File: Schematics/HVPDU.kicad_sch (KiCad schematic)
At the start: 11 parts, among them J35 BAMOCAR, J36 MCU CAN, J37 MCU COM, J38 3-2325013-1, J39 Energy Meter Current, J40 PL00X-301-10M8, J41 PL00Y-301-10M8, J42 HVD, J43 MCU Resolver, J44 Energy Meter Voltage, J45 Energy meter COM port

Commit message: Revise charger and HVPDU schematics
Updates the KiCad projects for Charger and Schematics with substantial schematic rework: replaces the AVR ISP header with a dedicated AVR-ISP-6 symbol, adjusts wiring/net labels and power symbols, adds new indicator/connectivity elements, and repositions components in HV iso and connector sheets. The HVPDU sheet is expanded to A3 and reorganized with additional connector/library symbol definitions and updated interconnect mapping. This commit also includes newly generated schematic backups and an exported HVPDU PDF.
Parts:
- added J46: DCDC HV side, symbol Connector_Generic:Conn_01x02
- added J47: DCDC LV Side, symbol Connector_Generic:Conn_01x02
- added J48: CCCV IN, symbol Connector_Generic:Conn_01x02
- added J49: CCCV OUT, symbol Connector_Generic:Conn_01x02
- added J50: RT00122PNH03, symbol Connector_Generic:Conn_01x02
- added J51: TSAL_R, symbol Connector_Generic:Conn_01x02
- added J52: TSMP+, symbol Connector_Generic:Conn_01x01
- added J53: TSMP-, symbol Connector_Generic:Conn_01x01
- added J54: GLVMP, symbol Connector_Generic:Conn_01x01
- added J57: DHAB S/106, symbol Connector_Generic:Conn_01x04
- added J58: 12V power plug, symbol Connector_Generic:Conn_01x08
- added J59: GND PLUG, symbol Connector_Generic:Conn_01x08
- added K6: DISCHARGE RELAY GIGAVAC PNC113BDA, symbol Relay:Relay_SPST-NC
- added R6: 1k5, symbol Device:R
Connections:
- net +12V: now also J45.4 (Pin_4), J58.1 (Pin_1), J58.2 (Pin_2), J58.3 (Pin_3), J58.4 (Pin_4), J58.5 (Pin_5), J58.6 (Pin_6), J58.7 (Pin_7), J58.8 (Pin_8); no longer J45.1 (Pin_1)
- net GND: now also J45.1 (Pin_1), J57.3 (Pin_3), J59.1 (Pin_1), J59.2 (Pin_2), J59.3 (Pin_3), J59.4 (Pin_4), J59.5 (Pin_5), J59.6 (Pin_6), J59.7 (Pin_7), J59.8 (Pin_8), K6.A2
- net SDC_Relay: now also K6.A1
- net TS+: now reaches J35.1 (Pin_1), J40.1 (Pin_1), J44.1 (Pin_1)
- net TS+: now also J46.1 (Pin_1), J51.1 (Pin_1), J52.1 (Pin_1), K6.12
- net TS-: now reaches J35.5 (Pin_5), J39.1 (Pin_1)
- net TS-: now also J46.2 (Pin_2), J51.2 (Pin_2), J53.1 (Pin_1), R6.1
- net FS_CAN_L: now reaches J45.2 (Pin_2)
- net FS_CAN_H: now reaches J45.3 (Pin_3)
- new net: J49.1 (Pin_1), J50.1 (Pin_1)
- new net: J49.2 (Pin_2), J50.2 (Pin_2)
- new net: J47.1 (Pin_1), J48.1 (Pin_1)
- new net: J47.2 (Pin_2), J48.2 (Pin_2)
- new net: K6.11, R6.2
- new net +5V: J57.1 (Pin_1)
- new net Current High: J57.2 (Pin_2)
- new net Current Low: J57.4 (Pin_4)
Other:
- note added: "Accum"
- note added: "BSPD"
- note added: "FS DATALOGGER"
- note added: "LVB"
- note added: "MCU Energy Meter TSAL_R TSAL_G"
- note added: "MCU Energy Meter TSAL_R TSAL_G GLVMP-"
- note added: "Main Hoop"
- note added: "Motor shit"
- note added: "VCU"
- moved on the sheet: J36, J37, J38, J43, J44, J45

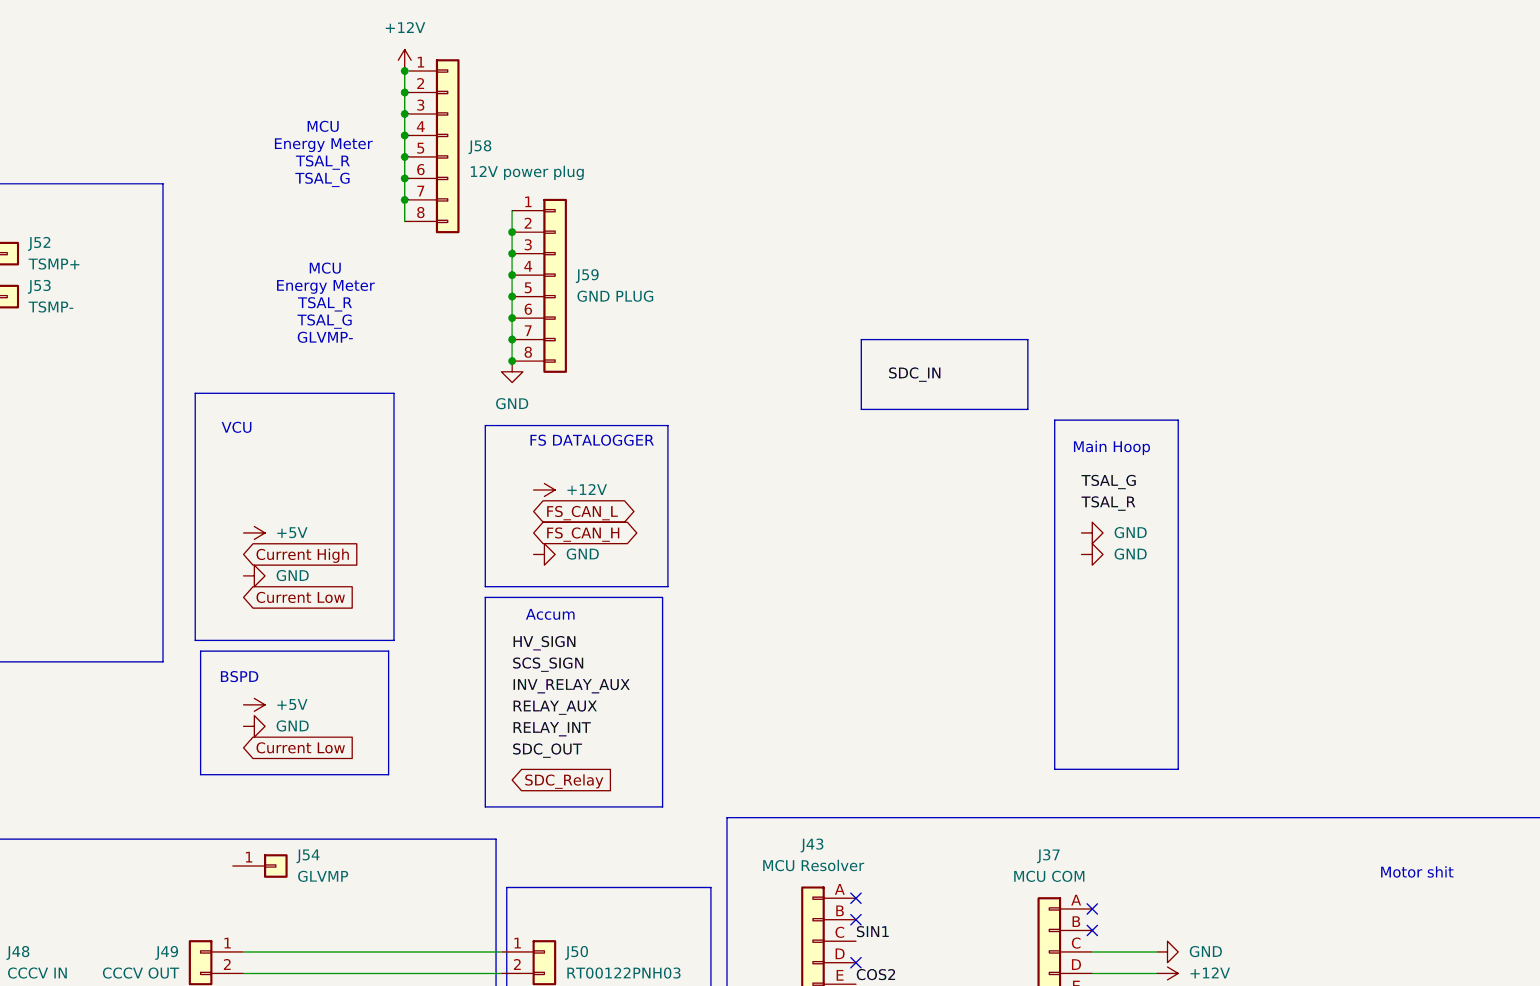
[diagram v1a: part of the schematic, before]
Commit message: Rework HVPDU and VCU connector wiring
Updates the HVPDU schematic with new connector symbols/instances (J55–J65), added MCU/FS CAN labels, and repositioned wiring blocks and labels. In VCU V3.3, the SRU/connector schematics and PCB were updated to reroute signals, rename the IGN_12V line to DIN_4, swap optocoupler value references to ELQ3H7, and realign many footprints/tracks; KiCad project metadata and 3D model references were also refreshed to KICAD10 paths. This change set also includes newly generated schematic backup ZIP archives.
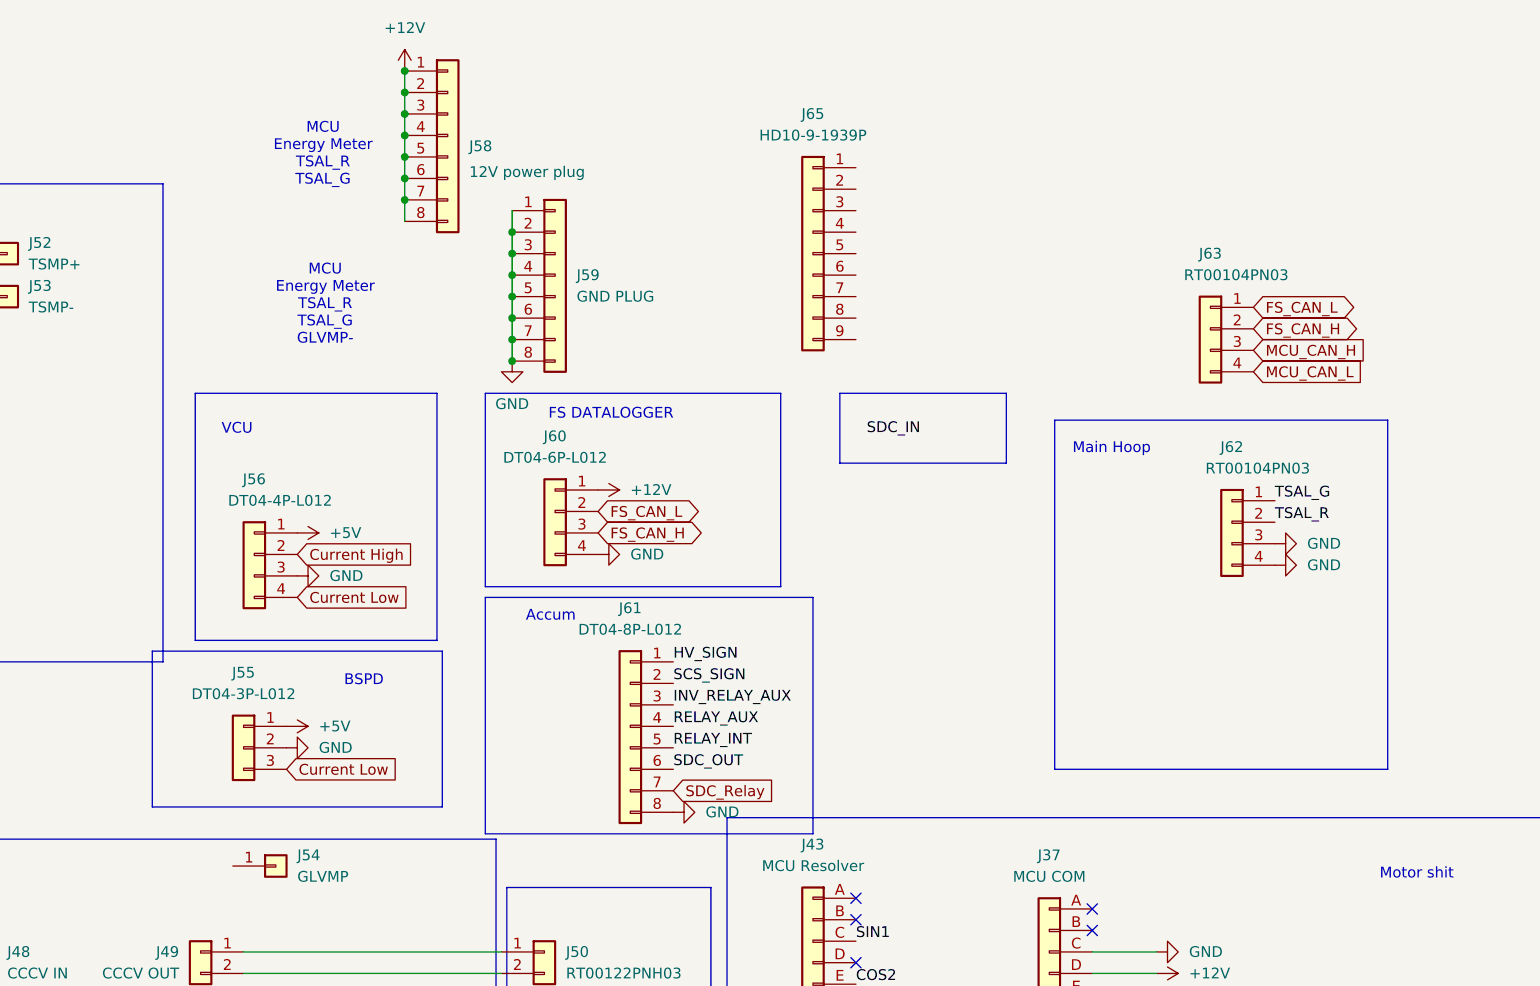
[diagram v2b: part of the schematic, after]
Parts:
- added J55: DT04-3P-L012, symbol Connector_Generic:Conn_01x03
- added J56: DT04-4P-L012, symbol Connector_Generic:Conn_01x04
- added J60: DT04-6P-L012, symbol Connector_Generic:Conn_01x04
- added J61: DT04-8P-L012, symbol Connector_Generic:Conn_01x08
- added J62, J63: RT00104PN03, symbol Connector_Generic:Conn_01x04
- added J65: HD10-9-1939P, symbol Connector_Generic:Conn_01x09
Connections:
- net +12V: now also J60.1 (Pin_1)
- net +5V: now also J55.1 (Pin_1), J56.1 (Pin_1)
- net Current High: now also J56.2 (Pin_2)
- net Current Low: now also J55.3 (Pin_3), J56.4 (Pin_4)
- net FS_CAN_H: now also J60.3 (Pin_3), J63.2 (Pin_2)
- net FS_CAN_L: now also J60.2 (Pin_2), J63.1 (Pin_1)
- net GND: now also J55.2 (Pin_2), J56.3 (Pin_3), J60.4 (Pin_4), J61.8 (Pin_8), J62.3 (Pin_3), J62.4 (Pin_4)
- net HV_SIGN: now also J61.1 (Pin_1)
- net INV_RELAY_AUX: now also J61.3 (Pin_3)
- net MCU_CAN_H: now also J63.3 (Pin_3)
- net MCU_CAN_L: now also J63.4 (Pin_4)
- net RELAY_AUX: now also J61.4 (Pin_4)
- net RELAY_INT: now also J61.5 (Pin_5)
- net SCS_SIGN: now also J61.2 (Pin_2)
- net SDC_OUT: now also J61.6 (Pin_6)
- net SDC_Relay: now also J61.7 (Pin_7)
- net TSAL_G: now also J62.1 (Pin_1)
- net TSAL_R: now also J62.2 (Pin_2)

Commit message: push stuffs
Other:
- moved on the sheet: J63
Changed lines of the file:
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@@
 	(global_label "FS_CAN_L"
 		(shape bidirectional)
-		(at 353.06 39.37 0)
-		(fields_autoplaced yes)
-		(effects
-			(font
-				(size 1.27 1.27)
-			)
-			(justify left)
-		)
-		(property "Intersheetrefs" "${INTERSHEET_REFS}"
-			(at 366.107 39.37 0)
+		(at 354.33 22.86 0)
+		(fields_autoplaced yes)
+		(effects
+			(font
+				(size 1.27 1.27)
+			)
+			(justify left)
+		)
+		(property "Intersheetrefs" "${INTERSHEET_REFS}"
+			(at 367.377 22.86 0)
 			(hide yes)
 			(show_name no)
@@
 	(global_label "MCU_CAN_L"
 		(shape input)
-		(at 353.06 46.99 0)
-		(fields_autoplaced yes)
-		(effects
-			(font
-				(size 1.27 1.27)
-			)
-			(justify left)
-		)
-		(property "Intersheetrefs" "${INTERSHEET_REFS}"
-			(at 366.7495 46.99 0)
+		(at 354.33 30.48 0)
+		(fields_autoplaced yes)
+		(effects
+			(font
+				(size 1.27 1.27)
+			)
+			(justify left)
+		)
+		(property "Intersheetrefs" "${INTERSHEET_REFS}"
+			(at 368.0195 30.48 0)
 			(hide yes)
 			(show_name no)
@@
 	(global_label "FS_CAN_H"
 		(shape bidirectional)
-		(at 353.06 41.91 0)
-		(fields_autoplaced yes)
-		(effects
-			(font
-				(size 1.27 1.27)
-			)
-			(justify left)
-		)
-		(property "Intersheetrefs" "${INTERSHEET_REFS}"
-			(at 366.4094 41.91 0)
+		(at 354.33 25.4 0)
+		(fields_autoplaced yes)
+		(effects
+			(font
+				(size 1.27 1.27)
+			)
+			(justify left)
+		)
+		(property "Intersheetrefs" "${INTERSHEET_REFS}"
+			(at 367.6794 25.4 0)
 			(hide yes)
 			(show_name no)
@@
 	(global_label "MCU_CAN_H"
 		(shape input)
-		(at 353.06 44.45 0)
-		(fields_autoplaced yes)
-		(effects
-			(font
-				(size 1.27 1.27)
-			)
-			(justify left)
-		)
-		(property "Intersheetrefs" "${INTERSHEET_REFS}"
-			(at 367.0519 44.45 0)
+		(at 354.33 27.94 0)
+		(fields_autoplaced yes)
+		(effects
+			(font
+				(size 1.27 1.27)
+			)
+			(justify left)
+		)
+		(property "Intersheetrefs" "${INTERSHEET_REFS}"
+			(at 368.3219 27.94 0)
 			(hide yes)
 			(show_name no)
@@
 	(symbol
 		(lib_id "Connector_Generic:Conn_01x04")
-		(at 347.98 41.91 0)
+		(at 349.25 25.4 0)
 		(mirror y)
 		(unit 1)
@@
 		(dnp no)
 		(property "Reference" "J63"
-			(at 347.98 33.02 0)
+			(at 349.25 16.51 0)
 			(show_name no)
 			(do_not_autoplace no)
@@
 		)
 		(property "Value" "RT00104PN03"
-			(at 351.028 35.56 0)
+			(at 352.298 19.05 0)
 			(show_name no)
 			(do_not_autoplace no)
@@
 		)
 		(property "Footprint" ""
-			(at 347.98 41.91 0)
+			(at 349.25 25.4 0)
 			(hide yes)
 			(show_name no)
@@
 		)
 		(property "Datasheet" ""
-			(at 347.98 41.91 0)
+			(at 349.25 25.4 0)
 			(hide yes)
 			(show_name no)
@@
 		)
 		(property "Description" "Generic connector, single row, 01x04, script generated (kicad-library-utils/schlib/autogen/connector/)"
-			(at 347.98 41.91 0)
-			(hide yes)
-			(show_name no)
+			(at 349.25 25.4 0)
+			(hide yes)
+			(show_name no)
